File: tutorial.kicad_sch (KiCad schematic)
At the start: 59 parts, among them J1 Conn_01x04_Socket, J2 Conn_01x02_Pin, J5 USB_C_Receptacle, J7 Conn_01x08_Socket, SW1 SW_SPDT, SW2 SW_Push, U1 AMS1117-3.3, U2 STM32F103C8T6, U3 MCP2542FD, Y2 ASCO

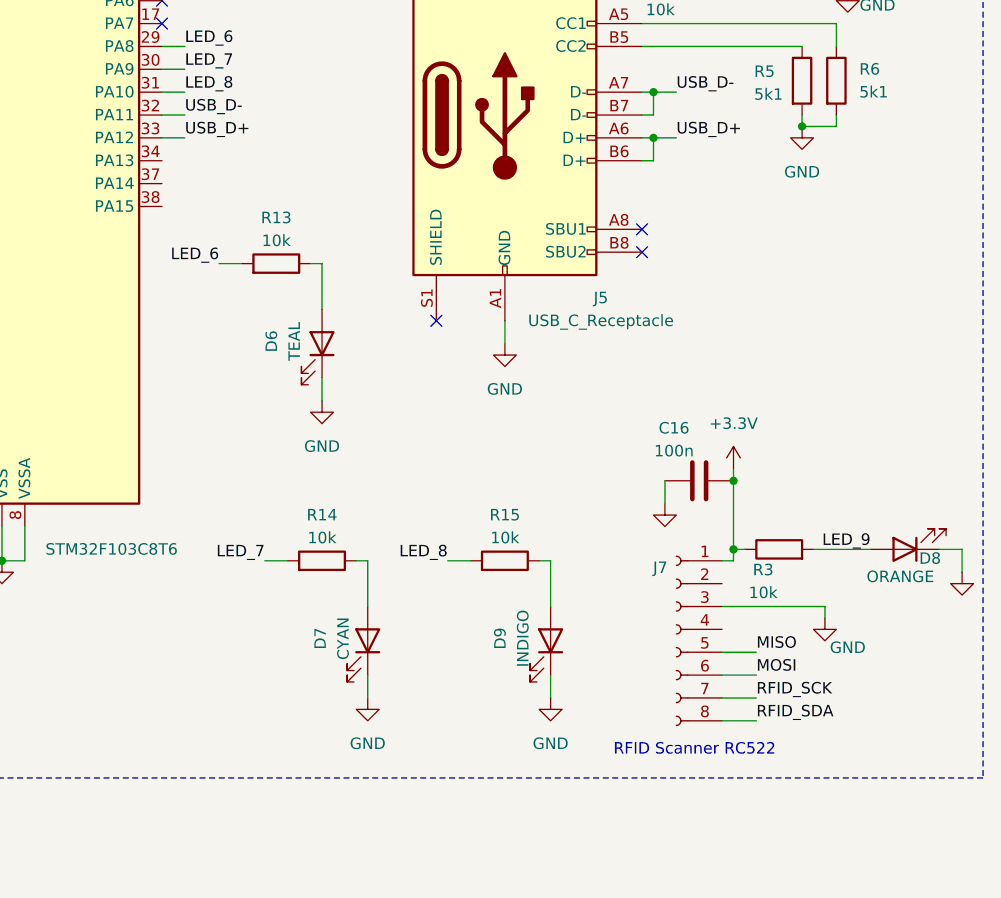
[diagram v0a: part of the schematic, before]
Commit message: Revised, added silkscreen
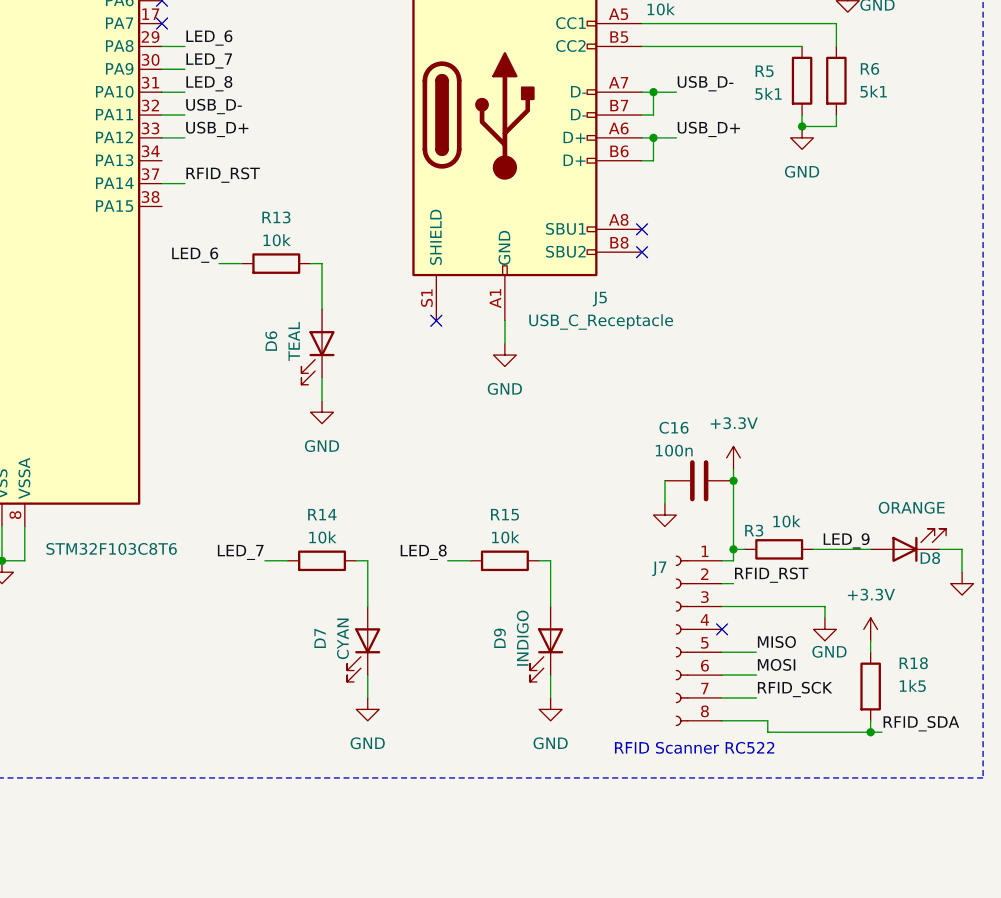
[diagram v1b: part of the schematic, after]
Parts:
- added R18: 1k5, Resistor_SMD:R_0603_1608Metric, symbol Device:R
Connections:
- net +3.3V: now also R18.1
- net RFID_SDA: now also R18.2
- net RFID_RST: now reaches U2.37 (PA14)
- net RFID_RST: now also J7.2 (Pin_2)
- no-connect marks 16 -> 17
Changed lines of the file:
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@@
 	)
 	(junction
+		(at 270.51 154.94)
+		(diameter 0)
+		(color 0 0 0 0)
+	)
+	(junction
 		(at 173.99 135.89)
 		(diameter 0)
@@
 	)
 	(no_connect
+		(at 254 143.51)
+	)
+	(no_connect
 		(at 191.77 71.12)
 	)
@@
 	(wire
 		(pts
+			(xy 270.51 154.94) (xy 259.08 154.94)
+		)
+		(stroke
+			(width 0)
+			(type default)
+		)
+	)
+	(wire
+		(pts
 			(xy 121.92 83.82) (xy 121.92 85.09)
 		)
@@
 	(wire
 		(pts
-			(xy 254 151.13) (xy 257.81 151.13)
-		)
-		(stroke
-			(width 0)
-			(type default)
-		)
-	)
-	(wire
-		(pts
 			(xy 246.38 88.9) (xy 248.92 88.9)
 		)
@@
 	(wire
 		(pts
+			(xy 191.77 93.98) (xy 194.31 93.98)
+		)
+		(stroke
+			(width 0)
+			(type default)
+		)
+	)
+	(wire
+		(pts
 			(xy 71.12 171.45) (xy 81.28 171.45)
 		)
@@
 	(wire
 		(pts
+			(xy 254 138.43) (xy 255.27 138.43)
+		)
+		(stroke
+			(width 0)
+			(type default)
+		)
+	)
+	(wire
+		(pts
 			(xy 99.06 124.46) (xy 100.33 124.46)
 		)
@@
 	(wire
 		(pts
+			(xy 271.78 154.94) (xy 270.51 154.94)
+		)
+		(stroke
+			(width 0)
+			(type default)
+		)
+	)
+	(wire
+		(pts
 			(xy 109.22 97.79) (xy 111.76 97.79)
 		)
@@
 	(wire
 		(pts
+			(xy 270.51 144.78) (xy 270.51 146.05)
+		)
+		(stroke
+			(width 0)
+			(type default)
+		)
+	)
+	(wire
+		(pts
 			(xy 191.77 88.9) (xy 194.31 88.9)
 		)
@@
 	(wire
 		(pts
+			(xy 259.08 154.94) (xy 259.08 153.67)
+		)
+		(stroke
+			(width 0)
+			(type default)
+		)
+	)
+	(wire
+		(pts
 			(xy 191.77 78.74) (xy 194.31 78.74)
 		)
@@
 	(wire
 		(pts
-			(xy 254 153.67) (xy 257.81 153.67)
+			(xy 254 153.67) (xy 259.08 153.67)
 		)
 		(stroke
@@
 	(wire
 		(pts
+			(xy 270.51 153.67) (xy 270.51 154.94)
+		)
+		(stroke
+			(width 0)
+			(type default)
+		)
+	)
+	(wire
+		(pts
 			(xy 52.07 85.09) (xy 57.15 85.09)
 		)
@@
 	(wire
 		(pts
+			(xy 254 151.13) (xy 257.81 151.13)
+		)
+		(stroke
+			(width 0)
+			(type default)
+		)
+	)
+	(wire
+		(pts
 			(xy 105.41 67.31) (xy 105.41 68.58)
 		)
@@
 	)
 	(label "RFID_SDA"
-		(at 257.81 153.67 0)
+		(at 271.78 154.94 0)
 		(effects
 			(font
@@
 		)
 	)
+	(label "RFID_RST"
+		(at 194.31 93.98 0)
+		(effects
+			(font
+				(size 1.27 1.27)
+			)
+			(justify left bottom)
+		)
+	)
 	(label "LED_4"
 		(at 140.97 138.43 0)
@@
 		)
 	)
+	(label "RFID_RST"
+		(at 255.27 138.43 0)
+		(effects
+			(font
+				(size 1.27 1.27)
+			)
+			(justify left bottom)
+		)
+	)
 	(label "CAN_RX"
 		(at 146.05 106.68 0)
@@
 		)
 		(property "Value" "ORANGE"
-			(at 273.812 137.668 0)
+			(at 275.082 130.048 0)
 			(effects
 				(font
@@
 	)
 	(symbol
+		(lib_id "Device:R")
+		(at 270.51 149.86 0)
+		(unit 1)
+		(exclude_from_sim no)
+		(in_bom yes)
+		(on_board yes)
+		(dnp no)
+		(property "Reference" "R18"
+			(at 273.558 147.32 0)
+			(effects
+				(font
+					(size 1.27 1.27)
+				)
+				(justify left)
+			)
+		)
+		(property "Value" "1k5"
+			(at 273.558 149.86 0)
+			(effects
+				(font
+					(size 1.27 1.27)
+				)
+				(justify left)
+			)
+		)
+		(property "Footprint" "Resistor_SMD:R_0603_1608Metric"
+			(at 268.732 149.86 90)
+			(effects
+				(font
+					(size 1.27 1.27)
+				)
+				(hide yes)
+			)
+		)
+		(property "Datasheet" "~"
+			(at 270.51 149.86 0)
+			(effects
+				(font
+					(size 1.27 1.27)
+				)
+				(hide yes)
+			)
+		)
+		(property "Description" "Resistor"
+			(at 270.51 149.86 0)
+			(effects
+				(font
+					(size 1.27 1.27)
+				)
+				(hide yes)
+			)
+		)
+		(pin "2"
+		)
+		(pin "1"
+		)
+		(instances
+			(project "tutorial"
+				(path "/e5ba5994-c558-424e-a7c8-18cd3f1acbf2"
+					(reference "R18")
+					(unit 1)
+				)
+			)
+		)
+	)
+	(symbol
 		(lib_id "Device:C")
 		(at 207.01 44.45 0)
@@
 		)
 		(property "Value" "GND"
-			(at 267.97 145.542 0)
+			(at 265.938 146.05 0)
 			(effects
 				(font
@@
 		(dnp no)
 		(property "Reference" "R3"
-			(at 258.572 136.906 90)
+			(at 257.556 132.588 90)
 			(effects
 				(font
@@
 		)
 		(property "Value" "10k"
-			(at 258.572 139.446 90)
+			(at 261.112 131.572 90)
 			(effects
 				(font
@@
 					(unit 1)
 				)
+			)
+		)
+	)
+	(symbol
+		(lib_id "power:+3.3V")
+		(at 270.51 144.78 0)
+		(unit 1)
+		(exclude_from_sim no)
+		(in_bom yes)
+		(on_board yes)
+		(dnp no)
+		(fields_autoplaced yes)
+		(property "Reference" "#PWR044"
+			(at 270.51 148.59 0)
+			(effects
+				(font
+					(size 1.27 1.27)
+				)
+				(hide yes)
+			)
+		)
+		(property "Value" "+3.3V"
+			(at 270.51 139.7 0)
+			(effects
+				(font
+					(size 1.27 1.27)
+				)
+			)
+		)
+		(property "Footprint" ""
+			(at 270.51 144.78 0)
+			(effects
+				(font
+					(size 1.27 1.27)
+				)
+				(hide yes)
+			)
+		)
+		(property "Datasheet" ""
+			(at 270.51 144.78 0)
+			(effects
+				(font
+					(size 1.27 1.27)
+				)
+				(hide yes)
+			)
+		)
+		(property "Description" "Power symbol creates a global label with name \"+3.3V\""
+			(at 270.51 144.78 0)
+			(effects
+				(font
+					(size 1.27 1.27)
+				)
+				(hide yes)
+			)
+		)
+		(pin "1"
+		)
+		(instances
+			(project "tutorial"
+				(path "/e5ba5994-c558-424e-a7c8-18cd3f1acbf2"
+					(reference "#PWR044")
+					(unit 1)
+				)

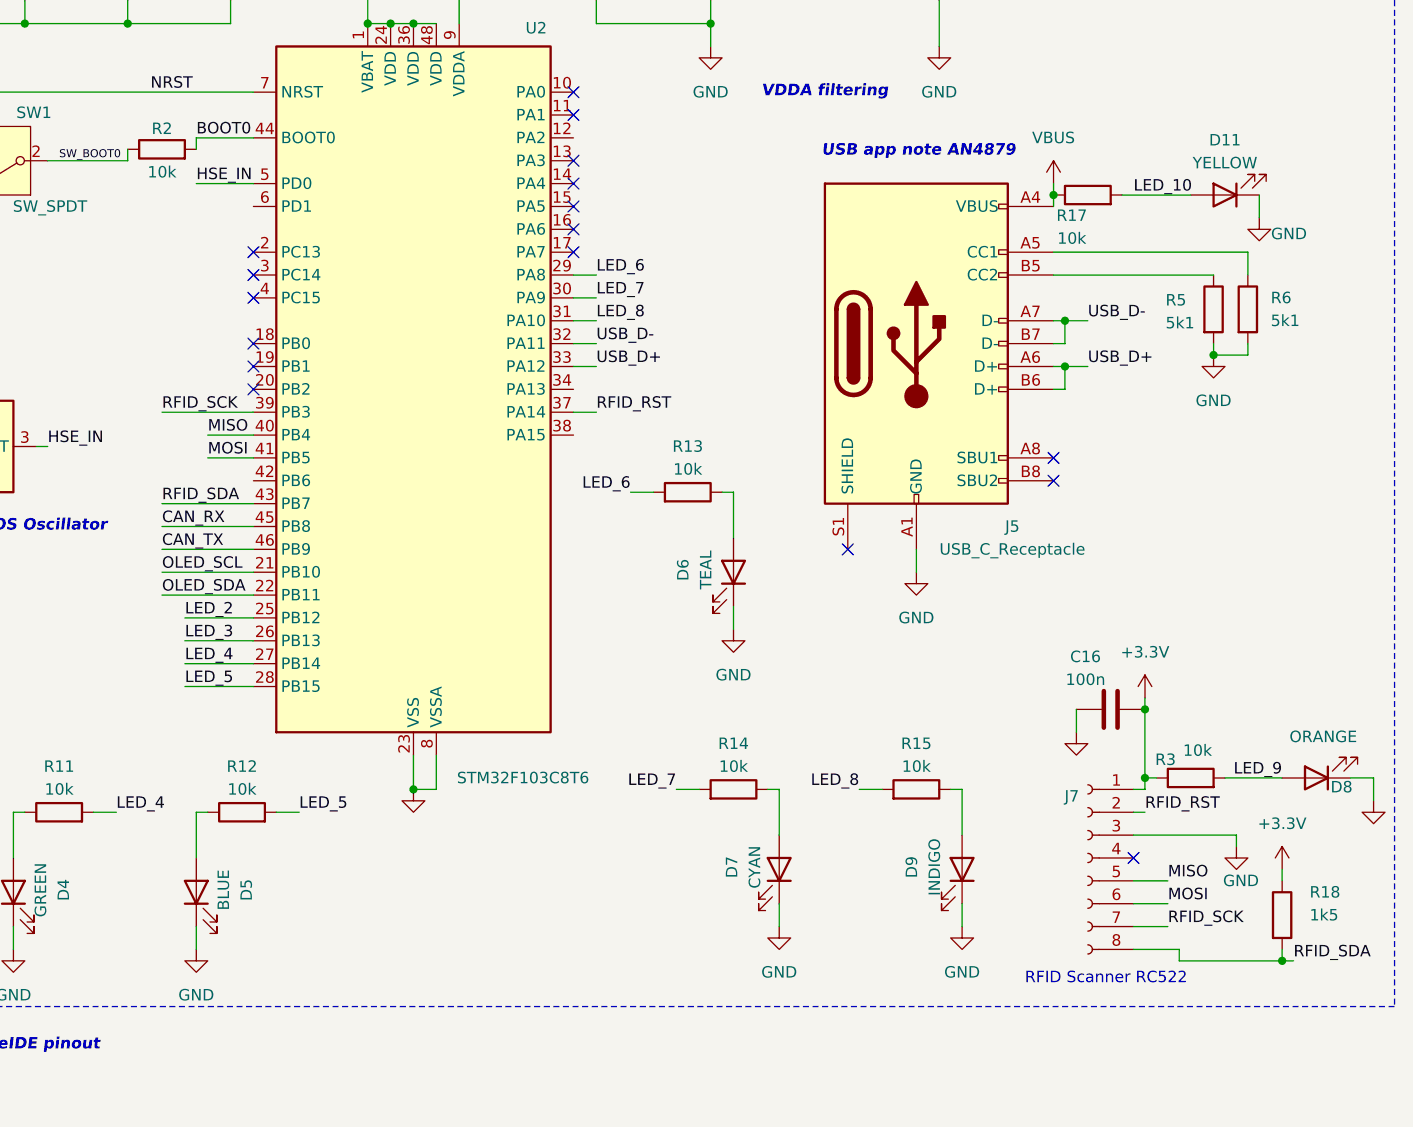
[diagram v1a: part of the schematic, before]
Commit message: Fix RFID pinout
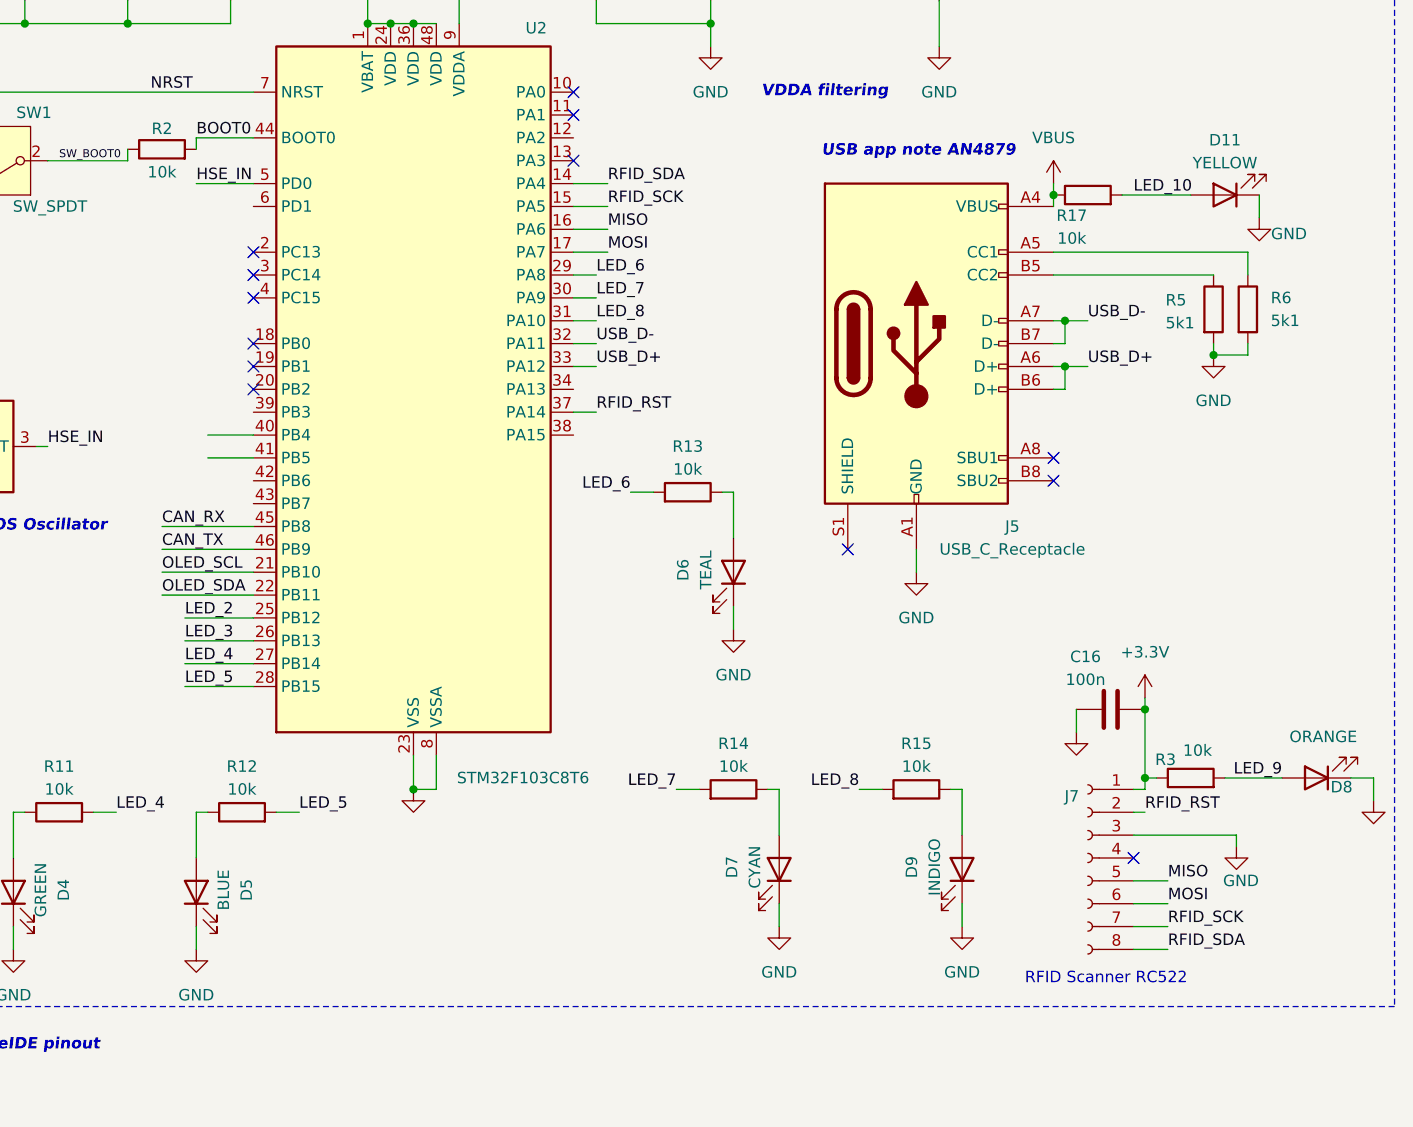
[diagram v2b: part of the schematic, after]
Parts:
- removed R18: 1k5, Resistor_SMD:R_0603_1608Metric, symbol Device:R
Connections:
- net MISO: now also U2.16 (PA6); no longer U2.40 (PB4)
- net MOSI: now also U2.17 (PA7); no longer U2.41 (PB5)
- net RFID_SCK: now also U2.15 (PA5); no longer U2.39 (PB3)
- net RFID_SDA: now also U2.14 (PA4); no longer U2.43 (PB7)
- no-connect marks 17 -> 13
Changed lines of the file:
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@@
 	)
 	(junction
-		(at 270.51 154.94)
-		(diameter 0)
-		(color 0 0 0 0)
-	)
-	(junction
 		(at 173.99 135.89)
 		(diameter 0)
@@
 	)
 	(no_connect
-		(at 191.77 71.12)
-	)
-	(no_connect
 		(at 156.21 76.2)
 	)
@@
 	)
 	(no_connect
-		(at 191.77 76.2)
-	)
-	(no_connect
 		(at 191.77 60.96)
 	)
 	(no_connect
-		(at 191.77 73.66)
-	)
-	(no_connect
 		(at 245.11 101.6)
 	)
@@
 		(at 222.25 109.22)
 	)
-	(no_connect
-		(at 191.77 68.58)
-	)
 	(wire
 		(pts
@@
 	(wire
 		(pts
-			(xy 270.51 154.94) (xy 259.08 154.94)
+			(xy 121.92 83.82) (xy 121.92 85.09)
 		)
 		(stroke
@@
 	(wire
 		(pts
-			(xy 121.92 83.82) (xy 121.92 85.09)
+			(xy 254 146.05) (xy 257.81 146.05)
 		)
 		(stroke
@@
 	(wire
 		(pts
-			(xy 254 146.05) (xy 257.81 146.05)
+			(xy 148.59 124.46) (xy 156.21 124.46)
 		)
 		(stroke
@@
 	(wire
 		(pts
-			(xy 148.59 124.46) (xy 156.21 124.46)
+			(xy 194.31 40.64) (xy 207.01 40.64)
 		)
 		(stroke
@@
 	(wire
 		(pts
-			(xy 194.31 40.64) (xy 207.01 40.64)
+			(xy 191.77 73.66) (xy 195.58 73.66)
 		)
 		(stroke
@@
 	(wire
 		(pts
+			(xy 191.77 76.2) (xy 195.58 76.2)
+		)
+		(stroke
+			(width 0)
+			(type default)
+		)
+	)
+	(wire
+		(pts
 			(xy 179.07 40.64) (xy 190.5 40.64)
 		)
@@
 	(wire
 		(pts
-			(xy 156.21 93.98) (xy 146.05 93.98)
-		)
-		(stroke
-			(width 0)
-			(type default)
-		)
-	)
-	(wire
-		(pts
 			(xy 190.5 40.64) (xy 194.31 40.64)
 		)
@@
 	(wire
 		(pts
-			(xy 271.78 154.94) (xy 270.51 154.94)
-		)
-		(stroke
-			(width 0)
-			(type default)
-		)
-	)
-	(wire
-		(pts
 			(xy 109.22 97.79) (xy 111.76 97.79)
 		)
@@
 	(wire
 		(pts
-			(xy 270.51 144.78) (xy 270.51 146.05)
-		)
-		(stroke
-			(width 0)
-			(type default)
-		)
-	)
-	(wire
-		(pts
 			(xy 191.77 88.9) (xy 194.31 88.9)
 		)
@@
 	(wire
 		(pts
-			(xy 259.08 154.94) (xy 259.08 153.67)
+			(xy 191.77 78.74) (xy 194.31 78.74)
 		)
 		(stroke
@@
 	(wire
 		(pts
-			(xy 191.77 78.74) (xy 194.31 78.74)
+			(xy 264.16 134.62) (xy 270.51 134.62)
 		)
 		(stroke
@@
 	(wire
 		(pts
-			(xy 264.16 134.62) (xy 270.51 134.62)
+			(xy 191.77 71.12) (xy 195.58 71.12)
 		)
 		(stroke
@@
 	(wire
 		(pts
-			(xy 254 153.67) (xy 259.08 153.67)
-		)
-		(stroke
-			(width 0)
-			(type default)
-		)
-	)
-	(wire
-		(pts
 			(xy 40.64 40.64) (xy 40.64 48.26)
 		)
@@
 	(wire
 		(pts
-			(xy 270.51 153.67) (xy 270.51 154.94)
-		)
-		(stroke
-			(width 0)
-			(type default)
-		)
-	)
-	(wire
-		(pts
 			(xy 52.07 85.09) (xy 57.15 85.09)
 		)
@@
 	(wire
 		(pts
-			(xy 146.05 104.14) (xy 156.21 104.14)
-		)
-		(stroke
-			(width 0)
-			(type default)
-		)
-	)
-	(wire
-		(pts
 			(xy 120.65 68.58) (xy 123.19 68.58)
 		)
@@
 	(wire
 		(pts
+			(xy 254 153.67) (xy 257.81 153.67)
+		)
+		(stroke
+			(width 0)
+			(type default)
+		)
+	)
+	(wire
+		(pts
 			(xy 138.43 138.43) (xy 140.97 138.43)
 		)
@@
 	(wire
 		(pts
+			(xy 191.77 68.58) (xy 195.58 68.58)
+		)
+		(stroke
+			(width 0)
+			(type default)
+		)
+	)
+	(wire
+		(pts
 			(xy 245.11 78.74) (xy 262.89 78.74)
 		)
@@
 	)
 	(label "MOSI"
-		(at 151.13 99.06 0)
+		(at 195.58 76.2 0)
 		(effects
 			(font
@@
 	)
 	(label "RFID_SCK"
-		(at 146.05 93.98 0)
+		(at 195.58 71.12 0)
 		(effects
 			(font
@@
 	)
 	(label "RFID_SDA"
-		(at 271.78 154.94 0)
+		(at 257.81 153.67 0)
 		(effects
 			(font
@@
 		)
 	)
+	(label "RFID_SDA"
+		(at 195.58 68.58 0)
+		(effects
+			(font
+				(size 1.27 1.27)
+			)
+			(justify left bottom)
+		)
+	)
 	(label "RFID_SCK"
 		(at 257.81 151.13 0)
@@
 	)
 	(label "MISO"
-		(at 151.13 96.52 0)
+		(at 195.58 73.66 0)
 		(effects
 			(font
@@
 		)
 	)
-	(label "RFID_SDA"
-		(at 146.05 104.14 0)
-		(effects
-			(font
-				(size 1.27 1.27)
-			)
-			(justify left bottom)
-		)
-	)
 	(label "PWR_LED_K"
 		(at 77.47 31.75 0)
@@
 	)
 	(symbol
-		(lib_id "Device:R")
-		(at 270.51 149.86 0)
-		(unit 1)
-		(exclude_from_sim no)
-		(in_bom yes)
-		(on_board yes)
-		(dnp no)
-		(property "Reference" "R18"
-			(at 273.558 147.32 0)
-			(effects
-				(font
-					(size 1.27 1.27)
-				)
-				(justify left)
-			)
-		)
-		(property "Value" "1k5"
-			(at 273.558 149.86 0)
-			(effects
-				(font
-					(size 1.27 1.27)
-				)
-				(justify left)
-			)
-		)
-		(property "Footprint" "Resistor_SMD:R_0603_1608Metric"
-			(at 268.732 149.86 90)
-			(effects
-				(font
-					(size 1.27 1.27)
-				)
-				(hide yes)
-			)
-		)
-		(property "Datasheet" "~"
-			(at 270.51 149.86 0)
-			(effects
-				(font
-					(size 1.27 1.27)
-				)
-				(hide yes)
-			)
-		)
-		(property "Description" "Resistor"
-			(at 270.51 149.86 0)
-			(effects
-				(font
-					(size 1.27 1.27)
-				)
-				(hide yes)
-			)
-		)
-		(pin "2"
-		)
-		(pin "1"
-		)
-		(instances
-			(project "tutorial"
-				(path "/e5ba5994-c558-424e-a7c8-18cd3f1acbf2"
-					(reference "R18")
-					(unit 1)
-				)
-			)
-		)
-	)
-	(symbol
 		(lib_id "Device:C")
 		(at 207.01 44.45 0)
@@
 					(unit 1)
 				)
-			)
-		)
-	)
-	(symbol
-		(lib_id "power:+3.3V")
-		(at 270.51 144.78 0)
-		(unit 1)
-		(exclude_from_sim no)
-		(in_bom yes)
-		(on_board yes)
-		(dnp no)
-		(fields_autoplaced yes)
-		(property "Reference" "#PWR044"
-			(at 270.51 148.59 0)
-			(effects
-				(font
-					(size 1.27 1.27)
-				)
-				(hide yes)
-			)
-		)
-		(property "Value" "+3.3V"
-			(at 270.51 139.7 0)
-			(effects
-				(font
-					(size 1.27 1.27)
-				)
-			)
-		)
-		(property "Footprint" ""
-			(at 270.51 144.78 0)
-			(effects
-				(font
-					(size 1.27 1.27)
-				)
-				(hide yes)
-			)
-		)
-		(property "Datasheet" ""
-			(at 270.51 144.78 0)
-			(effects
-				(font
-					(size 1.27 1.27)
-				)
-				(hide yes)
-			)
-		)
-		(property "Description" "Power symbol creates a global label with name \"+3.3V\""
-			(at 270.51 144.78 0)
-			(effects
-				(font
-					(size 1.27 1.27)
-				)
-				(hide yes)
-			)
-		)
-		(pin "1"
-		)
-		(instances
-			(project "tutorial"
-				(path "/e5ba5994-c558-424e-a7c8-18cd3f1acbf2"
-					(reference "#PWR044")
-					(unit 1)
-				)
